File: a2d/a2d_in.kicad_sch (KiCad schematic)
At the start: 11 parts, among them U1 B3B-XH-A(LF)(SN), U5 2060-453/998-404

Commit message: use 100nf
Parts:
- C18: value .1uf -> 100nf
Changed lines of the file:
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@@
 			)
 		)
-		(property "Value" ".1uf"
+		(property "Value" "100nf"
 			(at 63.5 49.5299 0)
 			(effects

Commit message: a2d v0.2
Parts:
- added JP1: Jumper_2_Small_Open, Connector_PinHeader_2.54mm:PinHeader_1x02_P2.54mm_Vertical, symbol Jumper:Jumper_2_Small_Open
- C1: renamed from C16; value 100nf -> 100nF
- C2: renamed from C18; value 100nf -> 100nF
- C3: renamed from C15; value 10uf -> 10uF
- C4: value 1uf -> 1uF
- R2: renamed from R4; value 100k -> 5.1M
- renumbered D2 to D1, FB4 to FB1, R5 to R1, U5 to U2
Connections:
- net GND: now also JP1.2 (B); no longer R2.1
- new net: JP1.1 (A), R2.1
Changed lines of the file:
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@@
 		(dnp no)
 		(fields_autoplaced yes)
-		(property "Reference" "#PWR024"
+		(property "Reference" "#PWR03"
 			(at 143.51 41.91 0)
 			(effects
@@
 		(dnp no)
 		(fields_autoplaced yes)
-		(property "Reference" "U5"
+		(property "Reference" "U2"
 			(at 91.44 40.6399 0)
 			(effects
@@
 		(dnp no)
 		(fields_autoplaced yes)
-		(property "Reference" "FB4"
+		(property "Reference" "FB1"
 			(at 73.7108 31.75 90)
 			(effects
@@
 		(dnp no)
 		(fields_autoplaced yes)
-		(property "Reference" "#PWR022"
+		(property "Reference" "#PWR04"
 			(at 76.2 41.91 0)
 			(effects
@@
 		(dnp no)
 		(fields_autoplaced yes)
-		(property "Reference" "#PWR023"
+		(property "Reference" "#PWR05"
 			(at 118.11 48.26 0)
 			(effects
@@
 		(dnp no)
 		(fields_autoplaced yes)
-		(property "Reference" "R5"
+		(property "Reference" "R1"
 			(at 58.42 33.02 90)
 			(effects
@@
 		(dnp no)
 		(fields_autoplaced yes)
-		(property "Reference" "C16"
+		(property "Reference" "C1"
 			(at 49.53 34.2899 0)
 			(effects
@@
 			)
 		)
-		(property "Value" "100nf"
+		(property "Value" "100nF"
 			(at 49.53 36.8299 0)
 			(effects
@@
 		(dnp no)
 		(fields_autoplaced yes)
-		(property "Reference" "C18"
+		(property "Reference" "C2"
 			(at 63.5 46.9899 0)
 			(effects
@@
 			)
 		)
-		(property "Value" "100nf"
+		(property "Value" "100nF"
 			(at 63.5 49.5299 0)
 			(effects
@@
 		(dnp no)
 		(fields_autoplaced yes)
-		(property "Reference" "#PWR021"
+		(property "Reference" "#PWR06"
 			(at 45.72 25.4 0)
 			(effects
@@
 	(symbol
 		(lib_id "power:GND")
+		(at 35.56 26.67 180)
+		(unit 1)
+		(exclude_from_sim no)
+		(in_bom yes)
+		(on_board yes)
+		(dnp no)
+		(fields_autoplaced yes)
+		(property "Reference" "#PWR07"
+			(at 35.56 20.32 0)
+			(effects
+				(font
+					(size 1.27 1.27)
+				)
+				(hide yes)
+			)
+		)
+		(property "Value" "GND"
+			(at 35.56 21.59 0)
+			(effects
+				(font
+					(size 1.27 1.27)
+				)
+			)
+		)
+		(property "Footprint" ""
+			(at 35.56 26.67 0)
+			(effects
+				(font
+					(size 1.27 1.27)
+				)
+				(hide yes)
+			)
+		)
+		(property "Datasheet" ""
+			(at 35.56 26.67 0)
+			(effects
+				(font
+					(size 1.27 1.27)
+				)
+				(hide yes)
+			)
+		)
+		(property "Description" "Power symbol creates a global label with name \"GND\" , ground"
+			(at 35.56 26.67 0)
+			(effects
+				(font
+					(size 1.27 1.27)
+				)
+				(hide yes)
+			)
+		)
+		(pin "1"
+		)
+		(instances
+			(project "a2d"
+				(path "/48ddfdd8-68fa-4e63-aa18-bc113cdf8cfa/232cd66d-546f-435c-bf9c-c78f53eeb560"
+					(reference "#PWR07")
+					(unit 1)
+				)
+				(path "/48ddfdd8-68fa-4e63-aa18-bc113cdf8cfa/b3d397fc-07a2-4d5d-89cf-6540d179c764"
+					(reference "#PWR030")
+					(unit 1)
+				)
+				(path "/48ddfdd8-68fa-4e63-aa18-bc113cdf8cfa/bb9ec583-ffe0-424f-8b73-f086e991deca"
+					(reference "#PWR020")
+					(unit 1)
+				)
+				(path "/48ddfdd8-68fa-4e63-aa18-bc113cdf8cfa/d0f4e225-c87a-4a52-8410-aab7f0d55970"
+					(reference "#PWR025")
+					(unit 1)
+				)
+			)
+		)
+	)
+	(symbol
+		(lib_id "power:GND")
 		(at 59.69 52.07 0)
 		(unit 1)
@@
 			)
 		)
-		(property "Value" "1uf"
+		(property "Value" "1uF"
 			(at 53.34 49.5299 0)
 			(effects
@@
 	)
 	(symbol
+		(lib_id "Jumper:Jumper_2_Small_Open")
+		(at 35.56 29.21 90)
+		(unit 1)
+		(exclude_from_sim yes)
+		(in_bom yes)
+		(on_board yes)
+		(dnp no)
+		(fields_autoplaced yes)
+		(property "Reference" "JP1"
+			(at 36.83 27.9399 90)
+			(effects
+				(font
+					(size 1.27 1.27)
+				)
+				(justify right)
+			)
+		)
+		(property "Value" "Jumper_2_Small_Open"
+			(at 36.83 30.4799 90)
+			(effects
+				(font
+					(size 1.27 1.27)
+				)
+				(justify right)
+				(hide yes)
+			)
+		)
+		(property "Footprint" "Connector_PinHeader_2.54mm:PinHeader_1x02_P2.54mm_Vertical"
+			(at 35.56 29.21 0)
+			(effects
+				(font
+					(size 1.27 1.27)
+				)
+				(hide yes)
+			)
+		)
+		(property "Datasheet" "~"
+			(at 35.56 29.21 0)
+			(effects
+				(font
+					(size 1.27 1.27)
+				)
+				(hide yes)
+			)
+		)
+		(property "Description" "Jumper, 2-pole, small symbol, open"
+			(at 35.56 29.21 0)
+			(effects
+				(font
+					(size 1.27 1.27)
+				)
+				(hide yes)
+			)
+		)
+		(pin "2"
+		)
+		(pin "1"
+		)
+		(instances
+			(project ""
+				(path "/48ddfdd8-68fa-4e63-aa18-bc113cdf8cfa/232cd66d-546f-435c-bf9c-c78f53eeb560"
+					(reference "JP1")
+					(unit 1)
+				)
+				(path "/48ddfdd8-68fa-4e63-aa18-bc113cdf8cfa/b3d397fc-07a2-4d5d-89cf-6540d179c764"
+					(reference "JP4")
+					(unit 1)
+				)
+				(path "/48ddfdd8-68fa-4e63-aa18-bc113cdf8cfa/bb9ec583-ffe0-424f-8b73-f086e991deca"
+					(reference "JP2")
+					(unit 1)
+				)
+				(path "/48ddfdd8-68fa-4e63-aa18-bc113cdf8cfa/d0f4e225-c87a-4a52-8410-aab7f0d55970"
+					(reference "JP3")
+					(unit 1)
+				)
+			)
+		)
+	)
+	(symbol
 		(lib_id "Device:R")
 		(at 35.56 35.56 0)
@@
 		(on_board yes)
 		(dnp no)
-		(fields_autoplaced yes)
-		(property "Reference" "R4"
+		(property "Reference" "R2"
 			(at 38.1 34.2899 0)
 			(effects
@@
 			)
 		)
-		(property "Value" "100k"
-			(at 38.1 36.8299 0)
+		(property "Value" "5.1M"
+			(at 38.1 36.83 0)
 			(effects
 				(font
@@
 		(dnp no)
 		(fields_autoplaced yes)
-		(property "Reference" "C15"
+		(property "Reference" "C3"
 			(at 41.91 46.9899 0)
 			(effects
@@
 			)
 		)
-		(property "Value" "10uf"
+		(property "Value" "10uF"
 			(at 41.91 49.5299 0)
 			(effects
@@
 	)
 	(symbol
-		(lib_id "power:GND")
-		(at 35.56 31.75 180)
-		(unit 1)
-		(exclude_from_sim no)
-		(in_bom yes)
-		(on_board yes)
-		(dnp no)
-		(fields_autoplaced yes)
-		(property "Reference" "#PWR020"
-			(at 35.56 25.4 0)
-			(effects
-				(font
-					(size 1.27 1.27)
-				)
-				(hide yes)
-			)
-		)
-		(property "Value" "GND"
-			(at 35.56 26.67 0)
-			(effects
-				(font
-					(size 1.27 1.27)
-				)
-			)
-		)
-		(property "Footprint" ""
-			(at 35.56 31.75 0)
-			(effects
-				(font
-					(size 1.27 1.27)
-				)
-				(hide yes)
-			)
-		)
-		(property "Datasheet" ""
-			(at 35.56 31.75 0)
-			(effects
-				(font
-					(size 1.27 1.27)
-				)
-				(hide yes)
-			)
-		)
-		(property "Description" "Power symbol creates a global label with name \"GND\" , ground"
-			(at 35.56 31.75 0)
-			(effects
-				(font
-					(size 1.27 1.27)
-				)
-				(hide yes)
-			)
-		)
-		(pin "1"
-		)
-		(instances
-			(project ""
-				(path "/48ddfdd8-68fa-4e63-aa18-bc113cdf8cfa/232cd66d-546f-435c-bf9c-c78f53eeb560"
-					(reference "#PWR07")
-					(unit 1)
-				)
-				(path "/48ddfdd8-68fa-4e63-aa18-bc113cdf8cfa/b3d397fc-07a2-4d5d-89cf-6540d179c764"
-					(reference "#PWR030")
-					(unit 1)
-				)
-				(path "/48ddfdd8-68fa-4e63-aa18-bc113cdf8cfa/bb9ec583-ffe0-424f-8b73-f086e991deca"
-					(reference "#PWR020")
-					(unit 1)
-				)
-				(path "/48ddfdd8-68fa-4e63-aa18-bc113cdf8cfa/d0f4e225-c87a-4a52-8410-aab7f0d55970"
-					(reference "#PWR025")
-					(unit 1)
-				)
-			)
-		)
-	)
-	(symbol
 		(lib_id "Power_Protection:RCLAMP0502B")
 		(at 123.19 41.91 0)
@@
 		(dnp no)
 		(fields_autoplaced yes)
-		(property "Reference" "D2"
+		(property "Reference" "D1"
 			(at 123.2535 33.02 0)
 			(effects

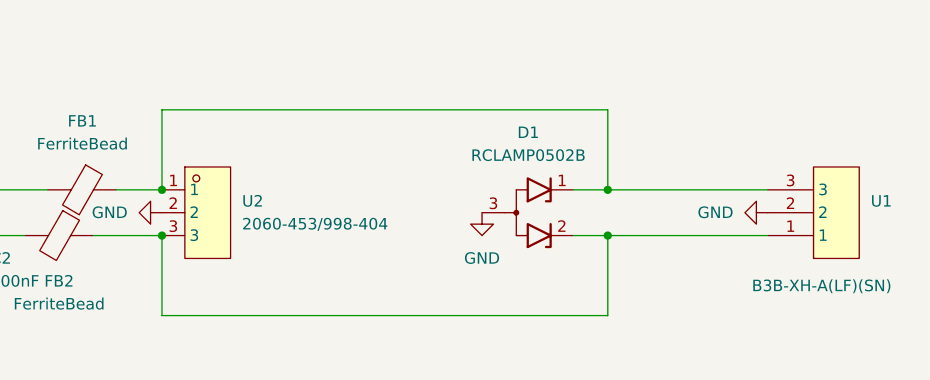
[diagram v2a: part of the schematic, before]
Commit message: reverse connector orientation for a2d
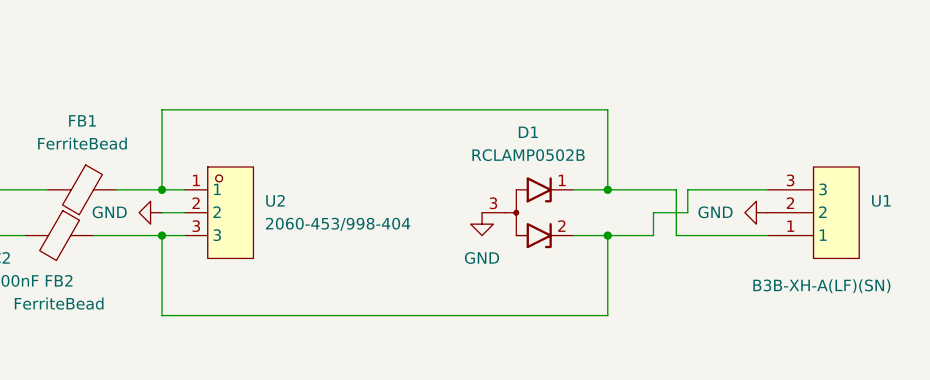
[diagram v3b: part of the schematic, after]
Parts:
- JP1: LCSC Part (none) -> C90288
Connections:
- net at D1.2 (K2), FB2.1, U2.3: now also U1.3; no longer U1.1
- net at D1.1 (K1), FB1.1, U2.1: now also U1.1; no longer U1.3
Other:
- moved on the sheet: U2
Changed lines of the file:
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@@
+	)
+	(junction
+		(at 59.69 44.45)
+		(diameter 0)
+		(color 0 0 0 0)
+	)
+	(junction
+		(at 82.55 39.37)
+		(diameter 0)
+		(color 0 0 0 0)
+	)
+	(junction
+		(at 45.72 39.37)
+		(diameter 0)
+		(color 0 0 0 0)
+	)
+	(junction
+		(at 132.08 39.37)
+		(diameter 0)
+		(color 0 0 0 0)
+	)
+	(junction
+		(at 38.1 44.45)
+		(diameter 0)
+		(color 0 0 0 0)
+	)
+	(junction
+		(at 35.56 39.37)
+		(diameter 0)
+		(color 0 0 0 0)
 	)
 	(junction
@@
 		(color 0 0 0 0)
 	)
-	(junction
-		(at 59.69 44.45)
-		(diameter 0)
-		(color 0 0 0 0)
-	)
-	(junction
-		(at 132.08 39.37)
-		(diameter 0)
-		(color 0 0 0 0)
-	)
-	(junction
-		(at 82.55 39.37)
-		(diameter 0)
-		(color 0 0 0 0)
-	)
-	(junction
-		(at 45.72 39.37)
-		(diameter 0)
-		(color 0 0 0 0)
-	)
-	(junction
-		(at 38.1 44.45)
-		(diameter 0)
-		(color 0 0 0 0)
-	)
-	(junction
-		(at 35.56 39.37)
-		(diameter 0)
-		(color 0 0 0 0)
-	)
 	(wire
 		(pts
@@
 	(wire
 		(pts
+			(xy 137.16 41.91) (xy 137.16 44.45)
+		)
+		(stroke
+			(width 0)
+			(type default)
+		)
+	)
+	(wire
+		(pts
+			(xy 85.09 41.91) (xy 82.55 41.91)
+		)
+		(stroke
+			(width 0)
+			(type default)
+		)
+	)
+	(wire
+		(pts
+			(xy 140.97 41.91) (xy 137.16 41.91)
+		)
+		(stroke
+			(width 0)
+			(type default)
+		)
+	)
+	(wire
+		(pts
 			(xy 35.56 39.37) (xy 45.72 39.37)
 		)
@@
 	(wire
 		(pts
+			(xy 139.7 44.45) (xy 139.7 39.37)
+		)
+		(stroke
+			(width 0)
+			(type default)
+		)
+	)
+	(wire
+		(pts
 			(xy 132.08 39.37) (xy 132.08 30.48)
 		)
@@
 	(wire
 		(pts
-			(xy 149.86 44.45) (xy 132.08 44.45)
-		)
-		(stroke
-			(width 0)
-			(type default)
-		)
-	)
-	(wire
-		(pts
 			(xy 132.08 30.48) (xy 82.55 30.48)
 		)
@@
 	(wire
 		(pts
+			(xy 140.97 39.37) (xy 140.97 41.91)
+		)
+		(stroke
+			(width 0)
+			(type default)
+		)
+	)
+	(wire
+		(pts
+			(xy 137.16 44.45) (xy 132.08 44.45)
+		)
+		(stroke
+			(width 0)
+			(type default)
+		)
+	)
+	(wire
+		(pts
 			(xy 45.72 39.37) (xy 54.61 39.37)
 		)
@@
 	(wire
 		(pts
+			(xy 149.86 39.37) (xy 140.97 39.37)
+		)
+		(stroke
+			(width 0)
+			(type default)
+		)
+	)
+	(wire
+		(pts
 			(xy 82.55 30.48) (xy 82.55 39.37)
 		)
@@
 	(wire
 		(pts
+			(xy 85.09 44.45) (xy 82.55 44.45)
+		)
+		(stroke
+			(width 0)
+			(type default)
+		)
+	)
+	(wire
+		(pts
 			(xy 74.93 44.45) (xy 82.55 44.45)
 		)
@@
 	(wire
 		(pts
+			(xy 149.86 44.45) (xy 139.7 44.45)
+		)
+		(stroke
+			(width 0)
+			(type default)
+		)
+	)
+	(wire
+		(pts
 			(xy 24.13 39.37) (xy 35.56 39.37)
 		)
@@
 	(wire
 		(pts
-			(xy 149.86 39.37) (xy 132.08 39.37)
-		)
-		(stroke
-			(width 0)
-			(type default)
-		)
-	)
-	(wire
-		(pts
 			(xy 77.47 39.37) (xy 82.55 39.37)
 		)
@@
 		(pts
 			(xy 59.69 44.45) (xy 67.31 44.45)
+		)
+		(stroke
+			(width 0)
+			(type default)
+		)
+	)
+	(wire
+		(pts
+			(xy 85.09 39.37) (xy 82.55 39.37)
+		)
+		(stroke
+			(width 0)
+			(type default)
+		)
+	)
+	(wire
+		(pts
+			(xy 132.08 39.37) (xy 139.7 39.37)
 		)
 		(stroke
@@
 		(shape input)
 		(at 24.13 44.45 180)
-		(fields_autoplaced yes)
 		(effects
 			(font
@@
 		(shape input)
 		(at 24.13 39.37 180)
-		(fields_autoplaced yes)
 		(effects
 			(font
@@
 	(symbol
 		(lib_id "easyeda2kicad:2060-453_998-404")
-		(at 87.63 41.91 0)
+		(at 90.17 41.91 0)
 		(unit 1)
 		(exclude_from_sim no)
@@
 		(fields_autoplaced yes)
 		(property "Reference" "U2"
-			(at 91.44 40.6399 0)
+			(at 93.98 40.6399 0)
 			(effects
 				(font
@@
 		)
 		(property "Value" "2060-453/998-404"
-			(at 91.44 43.1799 0)
+			(at 93.98 43.1799 0)
 			(effects
 				(font
@@
 		)
 		(property "Footprint" "easyeda2kicad:CONN-SMD_2060-453"
-			(at 87.63 52.07 0)
+			(at 90.17 52.07 0)
 			(effects
 				(font
@@
 		)
 		(property "Datasheet" ""
-			(at 87.63 41.91 0)
+			(at 90.17 41.91 0)
 			(effects
 				(font
@@
 		)
 		(property "Description" ""
-			(at 87.63 41.91 0)
+			(at 90.17 41.91 0)
 			(effects
 				(font
@@
 		)
 		(property "LCSC Part" "C2765056"
-			(at 87.63 54.61 0)
+			(at 90.17 54.61 0)
 			(effects
 				(font
@@
 			(effects
 				(font
+					(size 1.27 1.27)
+				)
+				(hide yes)
+			)
+		)
+		(property "LCSC Part" "C90288"
+			(at 35.56 29.21 90)
+			(effects
+				(font

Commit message: a2d v0.4
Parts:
- removed C3: 10uF, Capacitor_SMD:C_0603_1608Metric, symbol Device:C
- removed C4: 1uF, Capacitor_SMD:C_0603_1608Metric, symbol Device:C
- removed JP1: Jumper_2_Small_Open, Connector_PinHeader_2.54mm:PinHeader_1x02_P2.54mm_Vertical, symbol Jumper:Jumper_2_Small_Open
- removed U1: B3B-XH-A(LF)(SN), easyeda2kicad:CONN-TH_3P-P2.50_A2501WV2-3P, symbol easyeda2kicad:B3B-XH-A(LF)(SN)
- removed U2: 2060-453/998-404, easyeda2kicad:CONN-SMD_2060-453, symbol easyeda2kicad:2060-453_998-404
- added C17: 3.3uF, Capacitor_SMD:C_0603_1608Metric, symbol Device:C
- added CN3: 39302030, easyeda2kicad:CONN-TH_3P-P4.20_39302030, symbol easyeda2kicad:39302030
- renumbered C1 to C15, C2 to C18, D1 to D3, FB2 to FB1, FB1 to FB2, R1 to R3
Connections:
- net AOUT: now also C17.2
- net GND: now also R2.1, C17.1, CN3.3
- net at D3.1 (K1), FB2.1: now also CN3.2
- net at D3.2 (K2), FB1.1: now also CN3.1
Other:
- moved on the sheet: D3, FB1, FB2, R3
